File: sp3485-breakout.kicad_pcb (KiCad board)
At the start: 2 copper layers, 12.7 x 10.2 mm, 5 parts, among them J1 Conn_01x04, J2 Conn_01x04, U1 SP3485CN

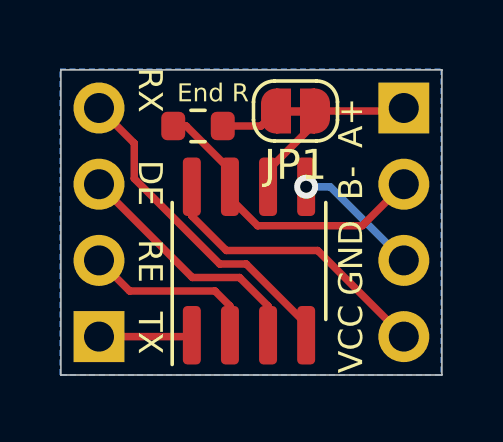
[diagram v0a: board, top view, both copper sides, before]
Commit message: Update silk and pad position
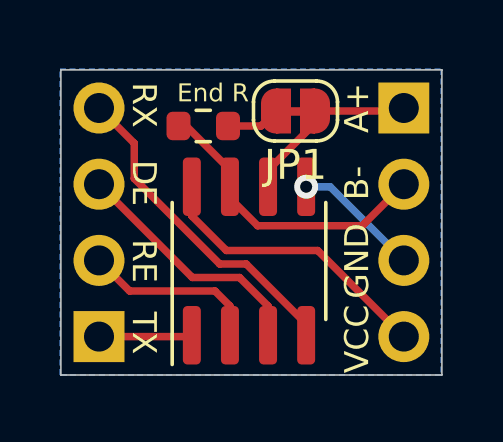
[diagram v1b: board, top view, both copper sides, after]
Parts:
- moved R1 0.17 mm to (151.5, 75.6)

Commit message: Update revision to 2020.11
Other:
- board text added: "Rev2020.11"
- board text removed: "Rev2020.10"
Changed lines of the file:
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@@
     )
   )
-  (gr_text Rev2020.10 (at 151.1 80.2 270) (layer B.SilkS)
+  (gr_text Rev2020.11 (at 151.1 80.2 270) (layer B.SilkS)
     (effects (font (size 0.8 0.8) (thickness 0.15)) (justify mirror))
   )
